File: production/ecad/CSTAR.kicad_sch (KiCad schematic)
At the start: 0 parts

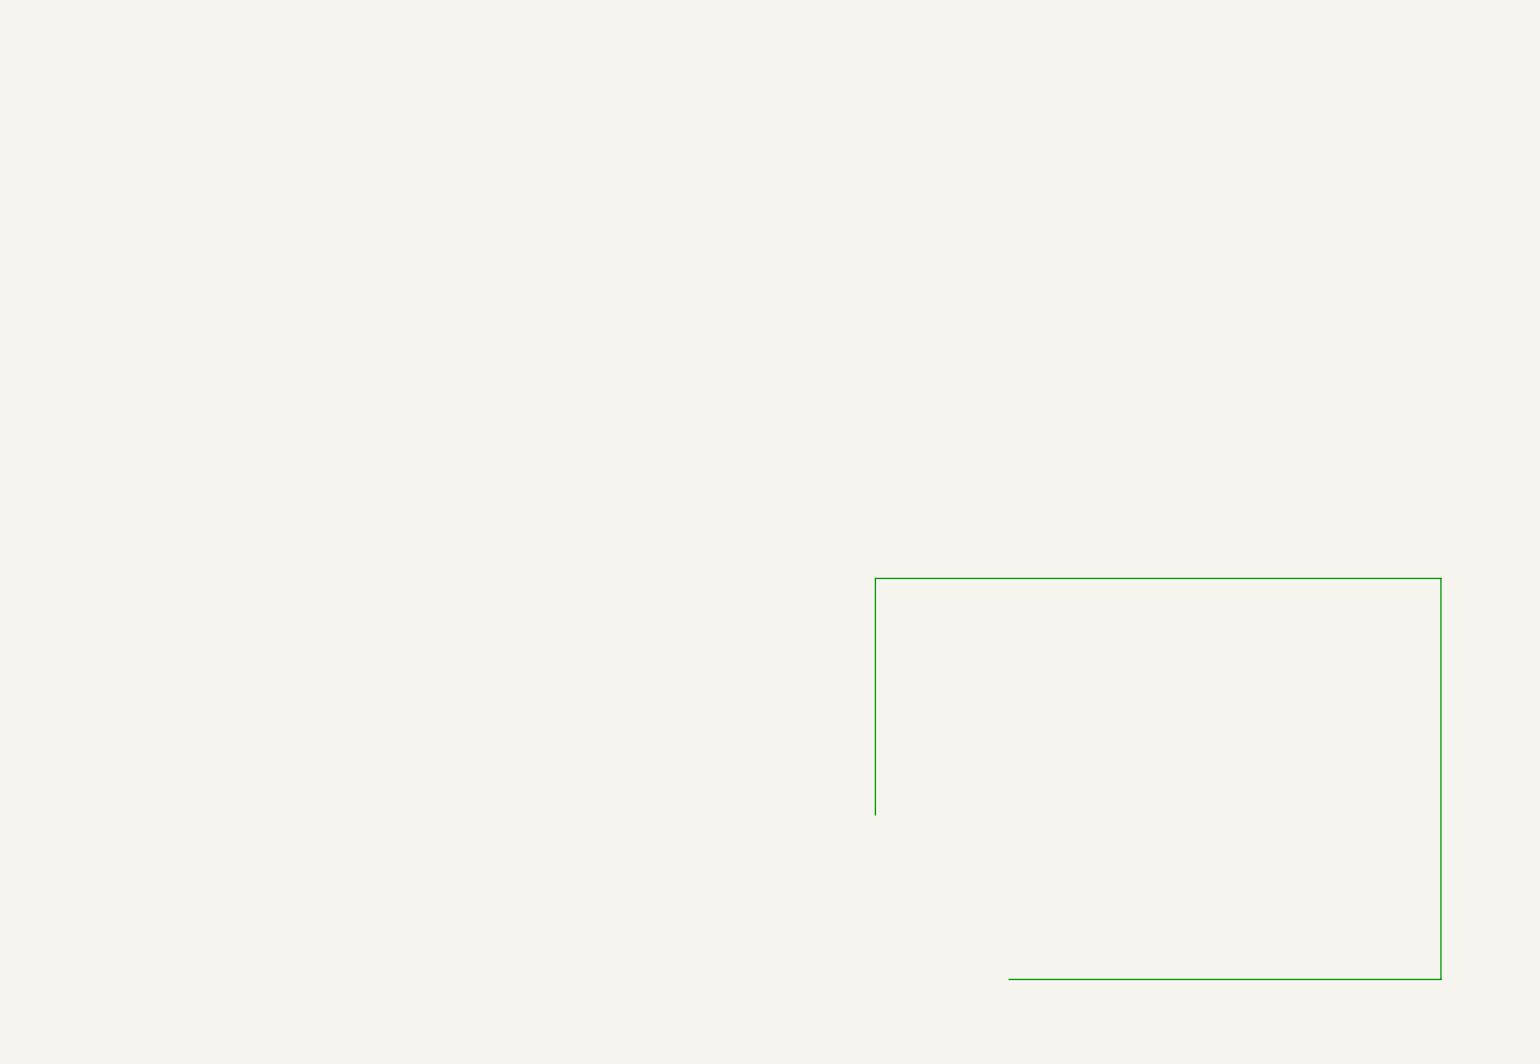
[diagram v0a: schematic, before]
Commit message: Added Hierarchical schematics!
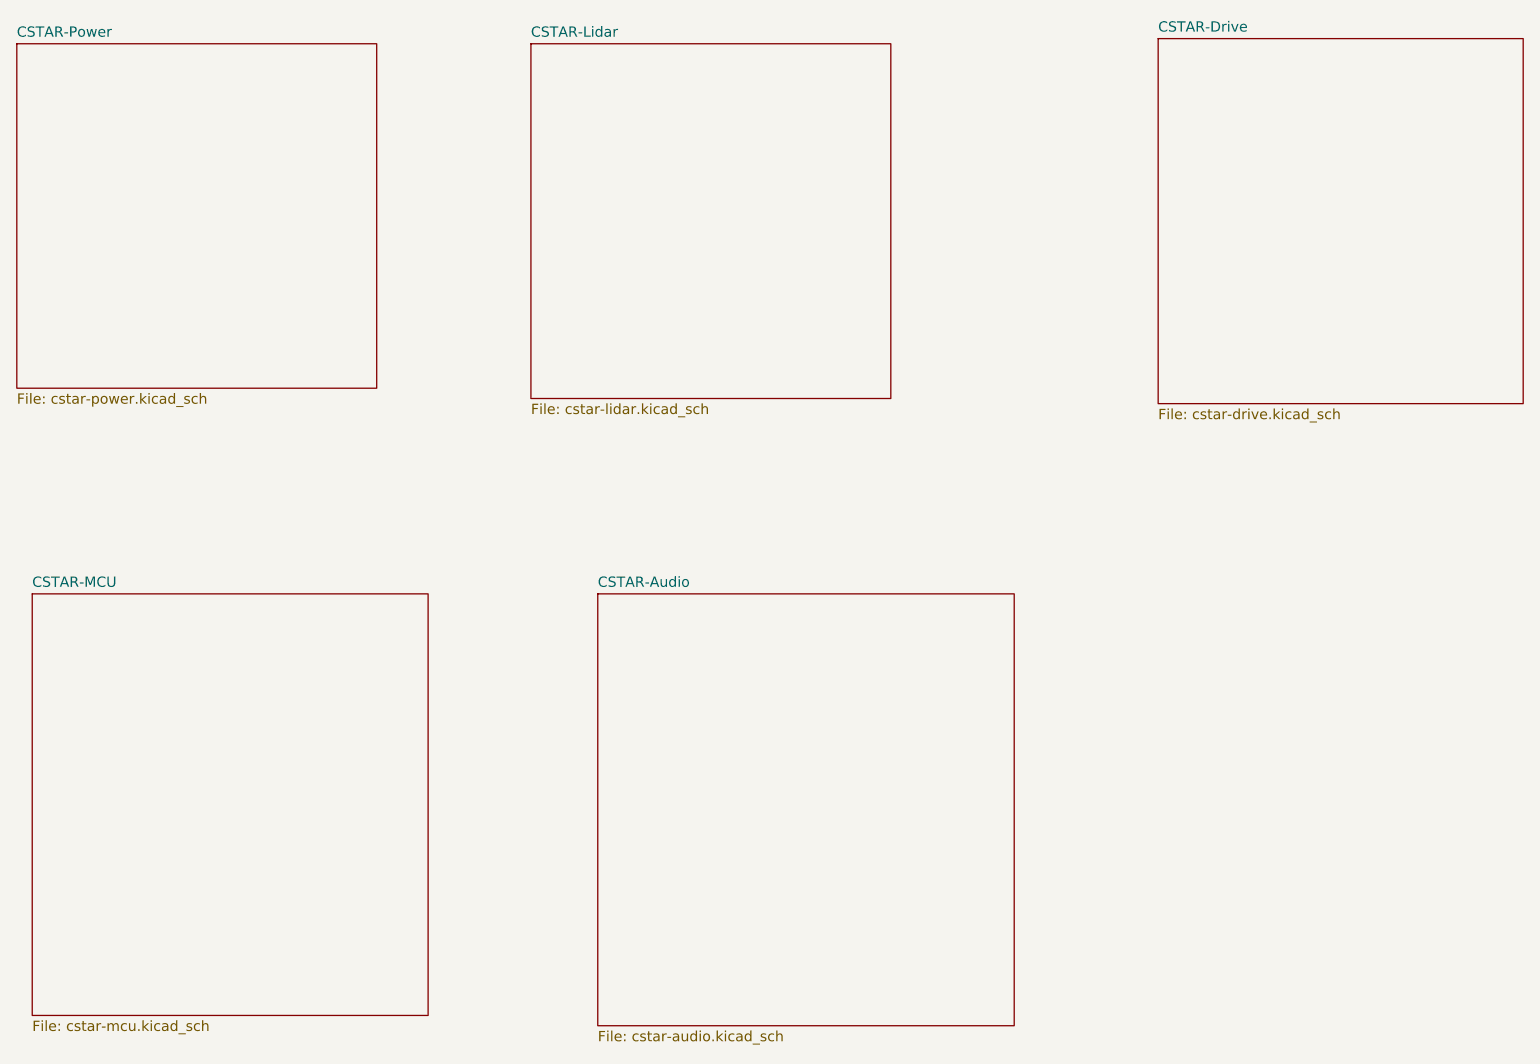
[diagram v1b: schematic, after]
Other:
- added sheet CSTAR-Audio (cstar-audio.kicad_sch)
- added sheet CSTAR-Drive (cstar-drive.kicad_sch)
- added sheet CSTAR-Lidar (cstar-lidar.kicad_sch)
- added sheet CSTAR-MCU (cstar-mcu.kicad_sch)
- added sheet CSTAR-Power (cstar-power.kicad_sch)
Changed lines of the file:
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@@
 (kicad_sch (version 20230121) (generator eeschema)
   (paper "A4")
-  (wire (pts (xy 144.78 125.73) (xy 144.78 96.52))
-    (stroke (width 0) (type default))
+  (sheet (at 38.735 30.48) (size 44.45 42.545) (fields_autoplaced)
+    (stroke (width 0.1524) (type solid))
+    (fill (color 0 0 0 0.0000))
+    (property "Sheetname" "CSTAR-Power" (at 38.735 29.7684 0)
+      (effects (font (size 1.27 1.27)) (justify left bottom))
+    )
+    (property "Sheetfile" "cstar-power.kicad_sch" (at 38.735 73.6096 0)
+      (effects (font (size 1.27 1.27)) (justify left top))
+    )
+    (instances
+      (project "CSTAR"
+        (path "/cd9fa943-c6eb-468b-990c-ea873c442553" (page "2"))
+      )
+    )
   )
-  (wire (pts (xy 214.63 146.05) (xy 161.29 146.05))
-    (stroke (width 0) (type default))
+  (sheet (at 110.49 98.425) (size 51.435 53.34) (fields_autoplaced)
+    (stroke (width 0.1524) (type solid))
+    (fill (color 0 0 0 0.0000))
+    (property "Sheetname" "CSTAR-Audio" (at 110.49 97.7134 0)
+      (effects (font (size 1.27 1.27)) (justify left bottom))
+    )
+    (property "Sheetfile" "cstar-audio.kicad_sch" (at 110.49 152.3496 0)
+      (effects (font (size 1.27 1.27)) (justify left top))
+    )
+    (instances
+      (project "CSTAR"
+        (path "/cd9fa943-c6eb-468b-990c-ea873c442553" (page "6"))
+      )
+    )
   )
-  (wire (pts (xy 214.63 96.52) (xy 214.63 146.05))
-    (stroke (width 0) (type default))
+  (sheet (at 102.235 30.48) (size 44.45 43.815) (fields_autoplaced)
+    (stroke (width 0.1524) (type solid))
+    (fill (color 0 0 0 0.0000))
+    (property "Sheetname" "CSTAR-Lidar" (at 102.235 29.7684 0)
+      (effects (font (size 1.27 1.27)) (justify left bottom))
+    )
+    (property "Sheetfile" "cstar-lidar.kicad_sch" (at 102.235 74.8796 0)
+      (effects (font (size 1.27 1.27)) (justify left top))
+    )
+    (instances
+      (project "CSTAR"
+        (path "/cd9fa943-c6eb-468b-990c-ea873c442553" (page "3"))
+      )
+    )
   )
-  (wire (pts (xy 144.78 96.52) (xy 214.63 96.52))
-    (stroke (width 0) (type default))
+  (sheet (at 179.705 29.845) (size 45.085 45.085) (fields_autoplaced)
+    (stroke (width 0.1524) (type solid))
+    (fill (color 0 0 0 0.0000))
+    (property "Sheetname" "CSTAR-Drive" (at 179.705 29.1334 0)
+      (effects (font (size 1.27 1.27)) (justify left bottom))
+    )
+    (property "Sheetfile" "cstar-drive.kicad_sch" (at 179.705 75.5146 0)
+      (effects (font (size 1.27 1.27)) (justify left top))
+    )
+    (instances
+      (project "CSTAR"
+        (path "/cd9fa943-c6eb-468b-990c-ea873c442553" (page "4"))
+      )
+    )
+  )
+  (sheet (at 40.64 98.425) (size 48.895 52.07) (fields_autoplaced)
+    (stroke (width 0.1524) (type solid))
+    (fill (color 0 0 0 0.0000))
+    (property "Sheetname" "CSTAR-MCU" (at 40.64 97.7134 0)
+      (effects (font (size 1.27 1.27)) (justify left bottom))
+    )
+    (property "Sheetfile" "cstar-mcu.kicad_sch" (at 40.64 151.0796 0)
+      (effects (font (size 1.27 1.27)) (justify left top))
+    )
+    (instances
+      (project "CSTAR"
+        (path "/cd9fa943-c6eb-468b-990c-ea873c442553" (page "5"))
+      )
+    )
   )
   (sheet_instances
